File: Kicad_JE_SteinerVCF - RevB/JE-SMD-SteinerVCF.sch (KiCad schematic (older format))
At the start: 55 parts, among them J201 HP, J202 BP, J203 LP, J204 Out, J205 CV, P201 Doepfer_Power_10pin, Q201 MMBT2907A, Q202 MMBT2222A, Q203 MMBT2222A, Q204 MMBT2222A

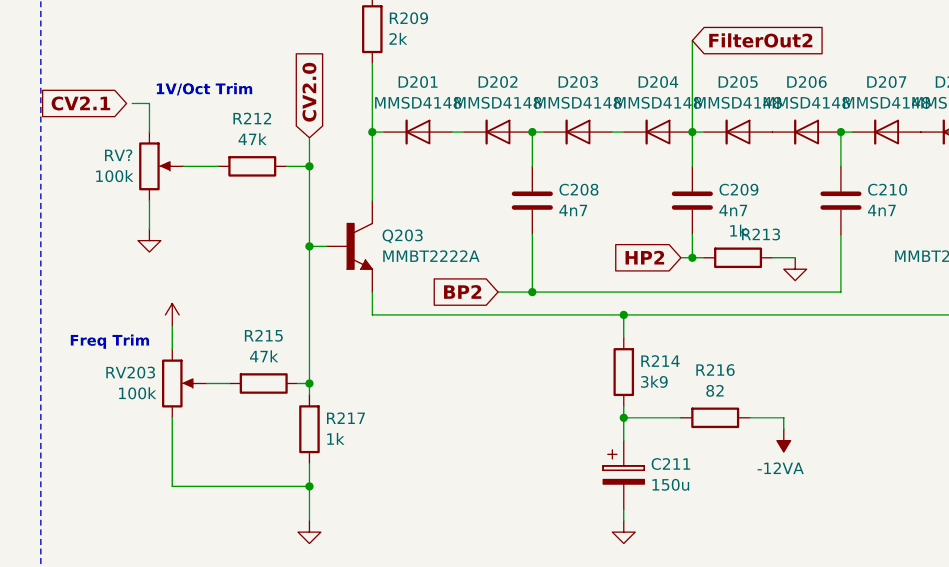
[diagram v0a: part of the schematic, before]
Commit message: VCF SMD
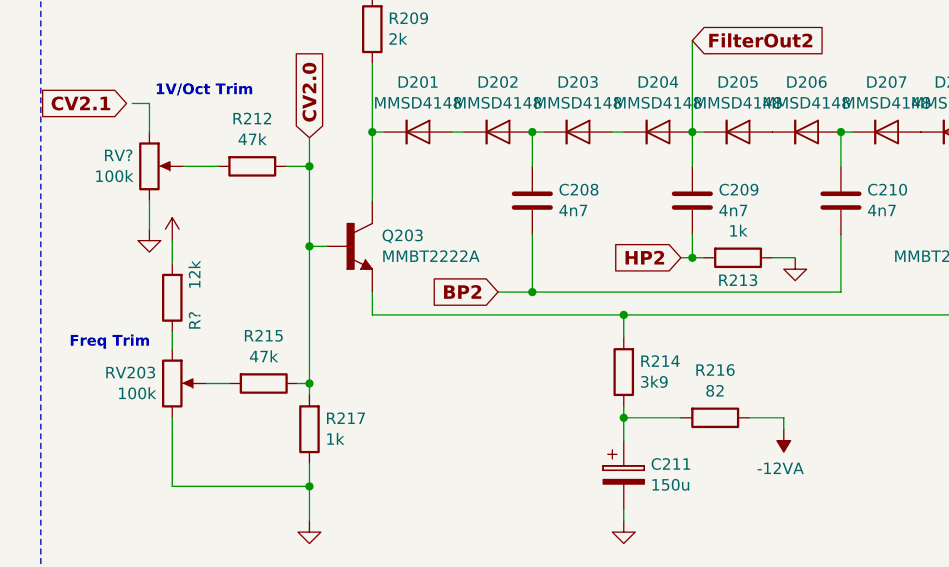
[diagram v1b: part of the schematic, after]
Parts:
- added R?: 12k, Resistor_SMD:R_0805_2012Metric_Pad1.15x1.40mm_HandSolder, symbol Device:R
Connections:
- net +12VA: now also R?.2; no longer RV203.1
- new net: R?.1, RV203.1
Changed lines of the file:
@@
 AR Path="/5C4E6289" Ref="R?"  Part="1"
 AR Path="/5C4E0953/5C4E6289" Ref="R213"  Part="1"
-F 0 "R213" V 3650 6300 50  0000 C CNN
+F 0 "R213" V 3850 6200 50  0000 C CNN
 F 1 "1k" V 3634 6200 50  0000 C CNN
 F 2 "Resistor_SMD:R_0805_2012Metric_Pad1.15x1.40mm_HandSolder" V 3680 6200 50  0001 C CNN
@@
 L power:+12VA #PWR?
 U 1 1 5C4E6304
-P 1275 6500
+P 1275 6125
 AR Path="/5C4E6304" Ref="#PWR?"  Part="1"
 AR Path="/5C4E0953/5C4E6304" Ref="#PWR0212"  Part="1"
-F 0 "#PWR0212" H 1275 6350 50  0001 C CNN
-F 1 "+12VA" H 1290 6673 50  0001 C CNN
-F 2 "" H 1275 6500 50  0001 C CNN
-F 3 "" H 1275 6500 50  0001 C CNN
-	1    1275 6500
-	1    0    0    -1
-$EndComp
-Wire Wire Line
-	1275 6600 1275 6500
+F 0 "#PWR0212" H 1275 5975 50  0001 C CNN
+F 1 "+12VA" H 1290 6298 50  0001 C CNN
+F 2 "" H 1275 6125 50  0001 C CNN
+F 3 "" H 1275 6125 50  0001 C CNN
+	1    1275 6125
+	1    0    0    -1
+$EndComp
 Text Notes 825  6600 0    47   ~ 9
 Freq Trim
@@
 Wire Wire Line
 	1900 2200 1900 2150
+$Comp
+L Device:R R?
+U 1 1 5CB8E54B
+P 1275 6375
+AR Path="/5CB8E54B" Ref="R?"  Part="1"
+AR Path="/5C4E0953/5CB8E54B" Ref="R?"  Part="1"
+F 0 "R?" V 1175 6475 50  0000 C CNN
+F 1 "12k" V 1175 6275 50  0000 C CNN
+F 2 "Resistor_SMD:R_0805_2012Metric_Pad1.15x1.40mm_HandSolder" V 1205 6375 50  0001 C CNN
+F 3 "~" H 1275 6375 50  0001 C CNN
+	1    1275 6375
+	-1   0    0    1
+$EndComp
+Wire Wire Line
+	1275 6125 1275 6225
+Wire Wire Line
+	1275 6525 1275 6600
 $EndSCHEMATC

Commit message: DRC RevB
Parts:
- gave numbers to parts that had none: 9
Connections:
- net CV2.1: now also RV202.1
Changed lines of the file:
@@
 EESchema Schematic File Version 4
 LIBS:Kicad_JE_SteinerVCF-cache
-EELAYER 26 0
+EELAYER 29 0
 EELAYER END
 $Descr A4 11693 8268
@@
 P 1175 5800
 AR Path="/5CB1D07D" Ref="RV?"  Part="1"
-AR Path="/5C4E0953/5CB1D07D" Ref="RV?"  Part="1"
-F 0 "RV?" H 1105 5846 50  0000 R CNN
+AR Path="/5C4E0953/5CB1D07D" Ref="RV202"  Part="1"
+F 0 "RV202" H 1105 5846 50  0000 R CNN
 F 1 "100k" H 1105 5755 50  0000 R CNN
 F 2 "AJ-Dropbox-Kicad:AlpsRK09K" H 1175 5800 50  0001 C CNN
@@
 $EndComp
 Wire Wire Line
-	1100 5525 1175 5525
-Wire Wire Line
 	1175 5525 1175 5650
 $Comp
@@
 P 1175 6075
 AR Path="/5CB24033" Ref="#PWR?"  Part="1"
-AR Path="/5C4E0953/5CB24033" Ref="#PWR?"  Part="1"
-F 0 "#PWR?" H 1175 5825 50  0001 C CNN
+AR Path="/5C4E0953/5CB24033" Ref="#PWR0216"  Part="1"
+F 0 "#PWR0216" H 1175 5825 50  0001 C CNN
 F 1 "GNDA" H 1180 5902 50  0001 C CNN
 F 2 "" H 1175 6075 50  0001 C CNN
@@
 P 6650 4050
 AR Path="/5CB6D1FC" Ref="R?"  Part="1"
-AR Path="/5C4E0953/5CB6D1FC" Ref="R?"  Part="1"
-F 0 "R?" V 6443 4050 50  0000 C CNN
+AR Path="/5C4E0953/5CB6D1FC" Ref="R218"  Part="1"
+F 0 "R218" V 6443 4050 50  0000 C CNN
 F 1 "47k" V 6534 4050 50  0000 C CNN
 F 2 "Resistor_SMD:R_0805_2012Metric_Pad1.15x1.40mm_HandSolder" V 6580 4050 50  0001 C CNN
@@
 P 6650 4450
 AR Path="/5CB6D49D" Ref="R?"  Part="1"
-AR Path="/5C4E0953/5CB6D49D" Ref="R?"  Part="1"
-F 0 "R?" V 6443 4450 50  0000 C CNN
+AR Path="/5C4E0953/5CB6D49D" Ref="R219"  Part="1"
+F 0 "R219" V 6443 4450 50  0000 C CNN
 F 1 "47k" V 6534 4450 50  0000 C CNN
 F 2 "Resistor_SMD:R_0805_2012Metric_Pad1.15x1.40mm_HandSolder" V 6580 4450 50  0001 C CNN
@@
 P 6650 4900
 AR Path="/5CB6D5FB" Ref="R?"  Part="1"
-AR Path="/5C4E0953/5CB6D5FB" Ref="R?"  Part="1"
-F 0 "R?" V 6443 4900 50  0000 C CNN
+AR Path="/5C4E0953/5CB6D5FB" Ref="R220"  Part="1"
+F 0 "R220" V 6443 4900 50  0000 C CNN
 F 1 "47k" V 6534 4900 50  0000 C CNN
 F 2 "Resistor_SMD:R_0805_2012Metric_Pad1.15x1.40mm_HandSolder" V 6580 4900 50  0001 C CNN
@@
 P 7125 4050
 AR Path="/5CB6D796" Ref="C?"  Part="1"
-AR Path="/5C4E0953/5CB6D796" Ref="C?"  Part="1"
-F 0 "C?" H 7240 4096 50  0000 L CNN
+AR Path="/5C4E0953/5CB6D796" Ref="C212"  Part="1"
+F 0 "C212" H 7240 4096 50  0000 L CNN
 F 1 "220n" H 7240 4005 50  0000 L CNN
 F 2 "Capacitor_SMD:C_0805_2012Metric_Pad1.15x1.40mm_HandSolder" H 7163 3900 50  0001 C CNN
@@
 P 7125 4450
 AR Path="/5CB6D9E9" Ref="C?"  Part="1"
-AR Path="/5C4E0953/5CB6D9E9" Ref="C?"  Part="1"
-F 0 "C?" H 7240 4496 50  0000 L CNN
+AR Path="/5C4E0953/5CB6D9E9" Ref="C213"  Part="1"
+F 0 "C213" H 7240 4496 50  0000 L CNN
 F 1 "470n" H 7240 4405 50  0000 L CNN
 F 2 "Capacitor_SMD:C_0805_2012Metric_Pad1.15x1.40mm_HandSolder" H 7163 4300 50  0001 C CNN
@@
 P 7125 4900
 AR Path="/5CB6DA81" Ref="C?"  Part="1"
-AR Path="/5C4E0953/5CB6DA81" Ref="C?"  Part="1"
-F 0 "C?" H 7240 4946 50  0000 L CNN
+AR Path="/5C4E0953/5CB6DA81" Ref="C214"  Part="1"
+F 0 "C214" H 7240 4946 50  0000 L CNN
 F 1 "1u" H 7240 4855 50  0000 L CNN
 F 2 "Capacitor_SMD:C_0805_2012Metric_Pad1.15x1.40mm_HandSolder" H 7163 4750 50  0001 C CNN
@@
 P 1900 2350
 AR Path="/5CB75FEC" Ref="R?"  Part="1"
-AR Path="/5C4E0953/5CB75FEC" Ref="R?"  Part="1"
-F 0 "R?" H 1830 2304 50  0000 R CNN
+AR Path="/5C4E0953/5CB75FEC" Ref="R211"  Part="1"
+F 0 "R211" H 1830 2304 50  0000 R CNN
 F 1 "82k" H 1830 2395 50  0000 R CNN
 F 2 "Resistor_SMD:R_0805_2012Metric_Pad1.15x1.40mm_HandSolder" V 1830 2350 50  0001 C CNN
@@
 P 1275 6375
 AR Path="/5CB8E54B" Ref="R?"  Part="1"
-AR Path="/5C4E0953/5CB8E54B" Ref="R?"  Part="1"
-F 0 "R?" V 1175 6475 50  0000 C CNN
+AR Path="/5C4E0953/5CB8E54B" Ref="R221"  Part="1"
+F 0 "R221" V 1175 6475 50  0000 C CNN
 F 1 "12k" V 1175 6275 50  0000 C CNN
 F 2 "Resistor_SMD:R_0805_2012Metric_Pad1.15x1.40mm_HandSolder" V 1205 6375 50  0001 C CNN
@@
 Wire Wire Line
 	1275 6525 1275 6600
+Wire Wire Line
+	1075 5525 1175 5525
 $EndSCHEMATC
